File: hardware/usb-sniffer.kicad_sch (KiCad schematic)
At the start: 40 parts, among them IC1 LCMXO2-2000HC-5TG100, IC2 MIC5504-3.3v, J1 USB-C, J2 USB-C, J3 USB-A, J4 IN, J5 GND

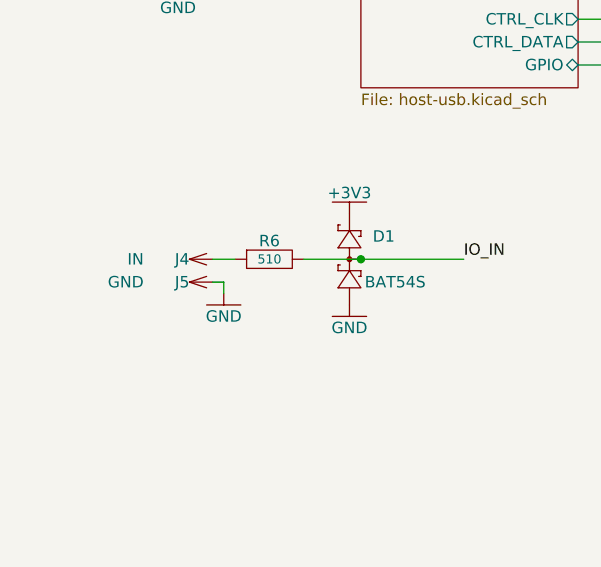
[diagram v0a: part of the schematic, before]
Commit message: Select parts for JLCPCB assembly
Also, modify USB type-A connector for an SMD part that is widely in
stocked.
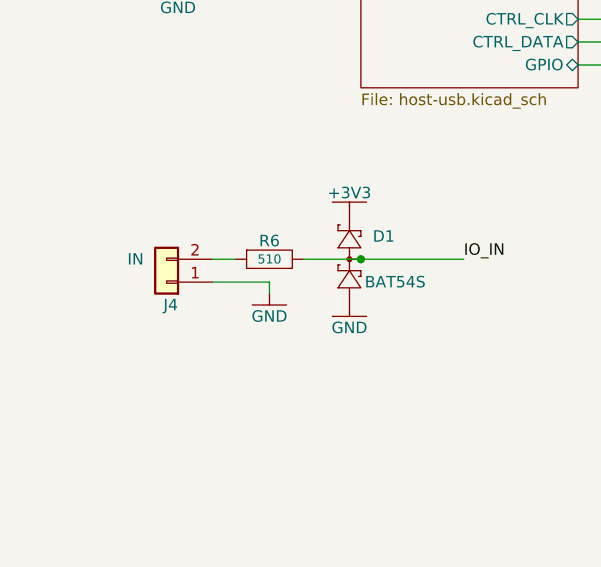
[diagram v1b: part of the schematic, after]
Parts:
- removed J5: GND, ataradov_conn:Pin-2.54mm, symbol ataradov_conn:Conn-Single
- C1, C2, C3, C4, C5, C6, C7, C8: LCSC (none) -> C14663
- C10, C9: LCSC (none) -> C15849
- D1: LCSC (none) -> C47546
- IC2: LCSC (none) -> C88419
- J1, J2: LCSC (none) -> C2835315
- J3: footprint ataradov_conn:USB-A-Slots -> usb-sniffer:C668591; LCSC (none) -> C668591
- J4: footprint ataradov_conn:Pin-2.54mm -> Connector_PinHeader_2.54mm:PinHeader_1x02_P2.54mm_Horizontal; symbol ataradov_conn:Conn-Single -> Connector_Generic:Conn_01x02; LCSC (none) -> C492410
- LED1: LCSC (none) -> C84264
- LED2, LED3, LED4, LED5: LCSC (none) -> C84269
- Logo1, TP1, TP2, TP3, TP4, TP5, TP6, TP7, TP8: now left out of the parts list
- R1, R2, R4, R5: LCSC (none) -> C23186
- R3, R7: LCSC (none) -> C25804
- R6: LCSC (none) -> C23193
- RN1: LCSC (none) -> C414564
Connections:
- net GND: now also J4.1 (Pin_1)
- net at R6.1: now also J4.2 (Pin_2); no longer J4.1

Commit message: Use LED_SMD:LED_0603_1608Metric footprint for LEDs
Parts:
- LED1, LED2, LED3, LED4, LED5: footprint ataradov_smd:0603 -> LED_SMD:LED_0603_1608Metric
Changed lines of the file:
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@@
       (effects (font (size 1.27 1.27)))
     )
-    (property "Footprint" "ataradov_smd:0603" (at 240.03 157.8864 0)
+    (property "Footprint" "LED_SMD:LED_0603_1608Metric" (at 240.03 157.8864 0)
       (effects (font (size 1.27 1.27)) hide)
     )
@@
       (effects (font (size 1.27 1.27)))
     )
-    (property "Footprint" "ataradov_smd:0603" (at 35.9664 97.79 0)
+    (property "Footprint" "LED_SMD:LED_0603_1608Metric" (at 35.9664 97.79 0)
       (effects (font (size 1.27 1.27)) hide)
     )
@@
       (effects (font (size 1.27 1.27)))
     )
-    (property "Footprint" "ataradov_smd:0603" (at 240.03 180.7464 0)
+    (property "Footprint" "LED_SMD:LED_0603_1608Metric" (at 240.03 180.7464 0)
       (effects (font (size 1.27 1.27)) hide)
     )
@@
       (effects (font (size 1.27 1.27)))
     )
-    (property "Footprint" "ataradov_smd:0603" (at 240.03 165.5064 0)
+    (property "Footprint" "LED_SMD:LED_0603_1608Metric" (at 240.03 165.5064 0)
       (effects (font (size 1.27 1.27)) hide)
     )
@@
       (effects (font (size 1.27 1.27)))
     )
-    (property "Footprint" "ataradov_smd:0603" (at 240.03 173.1264 0)
-      (effects (font (size 1.27 1.27)) hide)
-    )
+    (property "Footprint" "LED_SMD:LED_0603_1608Metric" (at 240.03 173.1264 0)
+      (effects (font (size 1.27 1.27)) hide)
+    )
